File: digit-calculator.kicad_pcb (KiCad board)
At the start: 2 copper layers, 38.5 x 45 mm, 5 parts, among them J1 Trackball, J2 Battery, SW1 Switch, U1 XIAO-ESP32-C3-SMD

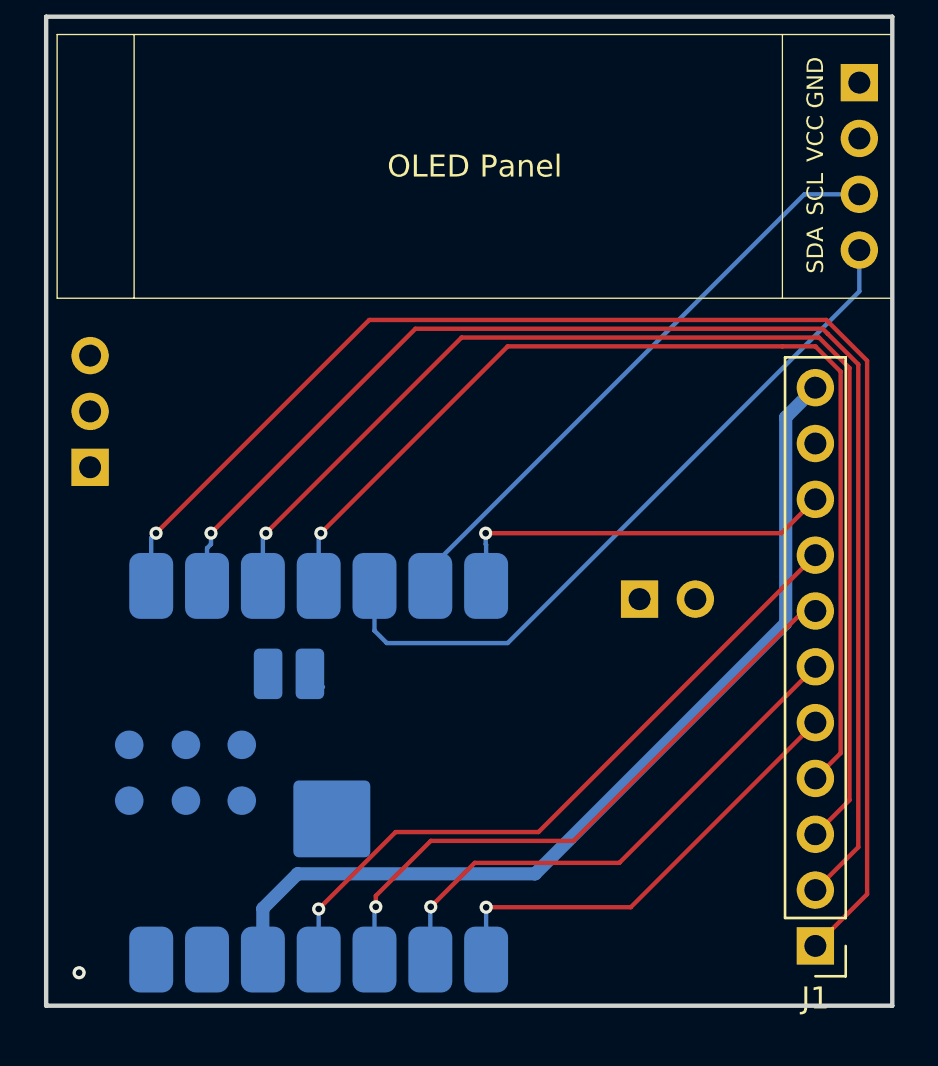
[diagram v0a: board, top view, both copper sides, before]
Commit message: Update wiring
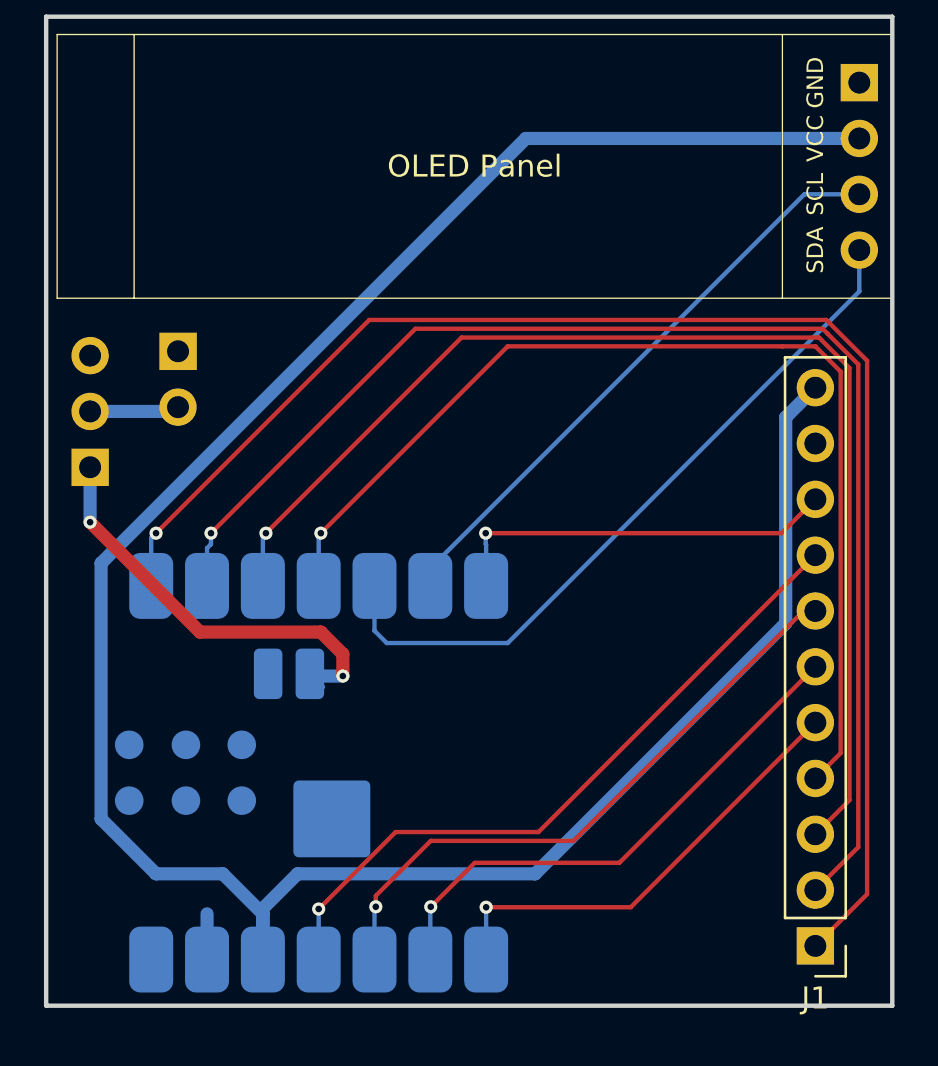
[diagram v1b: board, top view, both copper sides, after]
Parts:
- J2: value Battery -> - +
- moved J2 23.8 mm to (150.5, 64.7), turned to 180 degrees
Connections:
- SW1 pad 2: Net-(SW1-B) -> +BATT
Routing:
- net +3V3: track 42.8 -> 108.1 mm
- net +BATT: track 0.85 -> 24.0 mm, vias 0 -> 2
- net GND: track 0.00 -> 2.08 mm, vias 1 -> 0
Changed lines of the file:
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@@
 	(net 11 "/J_DOWN")
 	(net 12 "/J_RIGHT")
-	(net 13 "Net-(SW1-B)")
-	(net 14 "+BATT")
-	(net 15 "/SCL")
-	(net 16 "unconnected-(U1-VBUS-Pad14)")
+	(net 13 "+BATT")
+	(net 14 "/SCL")
+	(net 15 "unconnected-(U1-VBUS-Pad14)")
 	(footprint "Display:SSD1306-0.91-OLED-4pin-128x32"
 		(layer "F.Cu")
@@
 			(layers "*.Cu" "*.Mask")
 			(remove_unused_layers no)
-			(net 15 "/SCL")
+			(net 14 "/SCL")
 			(pinfunction "SCL")
 			(pintype "input")
@@
 	(footprint "Connector_PinHeader_2.54mm:PinHeader_1x02_P2.54mm_Vertical"
 		(layer "B.Cu")
-		(at 171.5 76 -90)
+		(at 150.5 64.725 180)
 		(descr "Through hole straight pin header, 1x02, 2.54mm pitch, single row")
 		(tags "Through hole pin header THT 1x02 2.54mm single row")
 		(property "Reference" "J2"
-			(at 0 2.38 90)
+			(at 0 2.38 0)
 			(layer "B.SilkS")
 			(effects
@@
 			)
 		)
-		(property "Value" "Battery"
-			(at 0 -4.92 90)
-			(layer "B.Fab")
-			(effects
-				(font
-					(size 1 1)
-					(thickness 0.15)
+		(property "Value" "- +"
+			(at -2.5 -1.275 90)
+			(layer "B.Fab")
+			(effects
+				(font
+					(size 1.4 1.4)
+					(thickness 0.175)
 				)
 				(justify mirror)
@@
 		)
 		(property "Datasheet" "~"
-			(at 0 0 90)
+			(at 0 0 0)
 			(layer "B.Fab")
 			(hide yes)
@@
 		)
 		(property "Description" "Generic connector, single row, 01x02, script generated (kicad-library-utils/schlib/autogen/connector/)"
-			(at 0 0 90)
+			(at 0 0 0)
 			(layer "B.Fab")
 			(hide yes)
@@
 		(attr through_hole)
 		(fp_line
+			(start 1.38 -1.27)
+			(end 1.38 -3.92)
+			(stroke
+				(width 0.12)
+				(type solid)
+			)
+			(layer "B.SilkS")
+		)
+		(fp_line
 			(start -1.38 1.38)
 			(end 0 1.38)
@@
 			(start -1.38 -1.27)
 			(end -1.38 -3.92)
-			(stroke
-				(width 0.12)
-				(type solid)
-			)
-			(layer "B.SilkS")
-		)
-		(fp_line
-			(start 1.38 -1.27)
-			(end 1.38 -3.92)
 			(stroke
 				(width 0.12)
@@
 		)
 		(fp_line
+			(start 1.27 1.27)
+			(end 1.27 -3.81)
+			(stroke
+				(width 0.1)
+				(type solid)
+			)
+			(layer "B.Fab")
+		)
+		(fp_line
+			(start 1.27 -3.81)
+			(end -1.27 -3.81)
+			(stroke
+				(width 0.1)
+				(type solid)
+			)
+			(layer "B.Fab")
+		)
+		(fp_line
 			(start -0.635 1.27)
 			(end 1.27 1.27)
@@
 		)
 		(fp_line
-			(start 1.27 1.27)
-			(end 1.27 -3.81)
-			(stroke
-				(width 0.1)
-				(type solid)
-			)
-			(layer "B.Fab")
-		)
-		(fp_line
 			(start -1.27 0.635)
 			(end -0.635 1.27)
@@
 			(layer "B.Fab")
 		)
-		(fp_line
-			(start 1.27 -3.81)
-			(end -1.27 -3.81)
-			(stroke
-				(width 0.1)
-				(type solid)
-			)
-			(layer "B.Fab")
-		)
 		(fp_text user "${REFERENCE}"
-			(at 0 -1.27 0)
+			(at 0 -1.27 90)
 			(layer "B.Fab")
 			(effects
@@
 		)
 		(pad "1" thru_hole rect
-			(at 0 0 270)
+			(at 0 0 180)
 			(size 1.7 1.7)
 			(drill 1)
@@
 		)
 		(pad "2" thru_hole circle
-			(at 0 -2.54 270)
+			(at 0 -2.54 180)
 			(size 1.7 1.7)
 			(drill 1)
 			(layers "*.Cu" "*.Mask")
 			(remove_unused_layers no)
-			(net 14 "+BATT")
+			(net 13 "+BATT")
 			(pinfunction "Pin_2")
 			(pintype "passive")
@@
 		)
 		(property "Value" "Switch"
-			(at 5 -5.5 0)
-			(layer "B.Fab")
+			(at -7 0.5 0)
+			(layer "B.Fab")
+			(hide yes)
 			(effects
 				(font
@@
 			(layers "*.Cu" "*.Mask")
 			(remove_unused_layers no)
-			(net 14 "+BATT")
+			(net 13 "+BATT")
 			(pinfunction "A")
 			(pintype "passive")
@@
 			(layers "*.Cu" "*.Mask")
 			(remove_unused_layers no)
-			(net 13 "Net-(SW1-B)")
+			(net 13 "+BATT")
 			(pinfunction "B")
 			(pintype "passive")
@@
 			(layers "B.Cu" "B.Mask" "B.Paste")
 			(roundrect_rratio 0.25)
-			(net 15 "/SCL")
+			(net 14 "/SCL")
 			(pinfunction "GPIO7_D5_SCL")
 			(pintype "passive")
@@
 			(layers "B.Cu" "B.Mask" "B.Paste")
 			(roundrect_rratio 0.25)
-			(net 16 "unconnected-(U1-VBUS-Pad14)")
+			(net 15 "unconnected-(U1-VBUS-Pad14)")
 			(pinfunction "VBUS")
 			(pintype "passive")
@@
 			(layers "B.Cu" "B.Mask" "B.Paste")
 			(roundrect_rratio 0.1923076923)
-			(net 14 "+BATT")
+			(net 13 "+BATT")
 		)
 		(pad "17" smd roundrect
@@
 		(layer "Edge.Cuts")
 	)
-	(via
-		(at 146 93)
-		(size 0.6)
-		(drill 0.3)
-		(layers "F.Cu" "B.Cu")
-		(free yes)
+	(segment
+		(start 151.82 92.4)
+		(end 151.82 90.32)
+		(width 0.6)
+		(layer "B.Cu")
 		(net 1)
+	)
+	(segment
+		(start 166.327214 55.04)
+		(end 147 74.367214)
+		(width 0.6)
+		(layer "B.Cu")
+		(net 2)
 	)
 	(segment
@@
 	)
 	(segment
+		(start 152.538 88.5)
+		(end 149.5 88.5)
+		(width 0.6)
+		(layer "B.Cu")
+		(net 2)
+	)
+	(segment
 		(start 178.149 67.731)
 		(end 179.5 66.38)
@@
 	)
 	(segment
-		(start 154.36 90.07855)
-		(end 155.93855 88.5)
+		(start 155.93855 88.5)
+		(end 154.36 90.07855)
 		(width 0.6)
 		(layer "B.Cu")
@@
 	)
 	(segment
+		(start 154.36 90.07855)
+		(end 154.36 92.4)
+		(width 0.6)
+		(layer "B.Cu")
+		(net 2)
+	)
+	(segment
 		(start 178.149 77.099603)
 		(end 178.149 67.731)
@@
 	)
 	(segment
-		(start 154.36 92.4)
-		(end 154.36 90.07855)
+		(start 147 74.367214)
+		(end 147 86)
+		(width 0.6)
+		(layer "B.Cu")
+		(net 2)
+	)
+	(segment
+		(start 181.5 55.04)
+		(end 166.327214 55.04)
+		(width 0.6)
+		(layer "B.Cu")
+		(net 2)
+	)
+	(segment
+		(start 154.36 90.322)
+		(end 154.36 92.4)
+		(width 0.6)
+		(layer "B.Cu")
+		(net 2)
+	)
+	(segment
+		(start 149.5 88.5)
+		(end 147 86)
+		(width 0.6)
+		(layer "B.Cu")
+		(net 2)
+	)
+	(segment
+		(start 152.538 88.5)
+		(end 154.36 90.322)
 		(width 0.6)
 		(layer "B.Cu")
@@
 	)
 	(segment
+		(start 151.5 77.5)
+		(end 157 77.5)
+		(width 0.6)
+		(layer "F.Cu")
+		(net 13)
+	)
+	(segment
+		(start 158 78.5)
+		(end 158 79.5)
+		(width 0.6)
+		(layer "F.Cu")
+		(net 13)
+	)
+	(segment
+		(start 146.5 72.5)
+		(end 151.5 77.5)
+		(width 0.6)
+		(layer "F.Cu")
+		(net 13)
+	)
+	(segment
+		(start 157 77.5)
+		(end 158 78.5)
+		(width 0.6)
+		(layer "F.Cu")
+		(net 13)
+	)
+	(via
+		(at 146.5 72.5)
+		(size 0.6)
+		(drill 0.3)
+		(layers "F.Cu" "B.Cu")
+		(net 13)
+	)
+	(via
+		(at 158 79.5)
+		(size 0.6)
+		(drill 0.3)
+		(layers "F.Cu" "B.Cu")
+		(free yes)
+		(net 13)
+	)
+	(segment
+		(start 150.305 67.46)
+		(end 150.5 67.265)
+		(width 0.6)
+		(layer "B.Cu")
+		(net 13)
+	)
+	(segment
+		(start 156.6 79.5)
+		(end 156.5 79.4)
+		(width 0.6)
+		(layer "B.Cu")
+		(net 13)
+	)
+	(segment
+		(start 158 79.5)
+		(end 156.6 79.5)
+		(width 0.6)
+		(layer "B.Cu")
+		(net 13)
+	)
+	(segment
 		(start 156.5 79.4)
 		(end 157.1 80)
 		(width 0.2)
 		(layer "B.Cu")
-		(net 14)
+		(net 13)
+	)
+	(segment
+		(start 146.5 67.46)
+		(end 150.305 67.46)
+		(width 0.6)
+		(layer "B.Cu")
+		(net 13)
+	)
+	(segment
+		(start 146.5 70)
+		(end 146.5 72.5)
+		(width 0.6)
+		(layer "B.Cu")
+		(net 13)
 	)
 	(segment
@@
 		(width 0.2)
 		(layer "B.Cu")
-		(net 15)
+		(net 14)
 	)
 	(segment
@@
 		(width 0.2)
 		(layer "B.Cu")
-		(net 15)
+		(net 14)
 	)
 	(segment
@@
 		(width 0.2)
 		(layer "B.Cu")
-		(net 15)
+		(net 14)
 	)
 	(zone

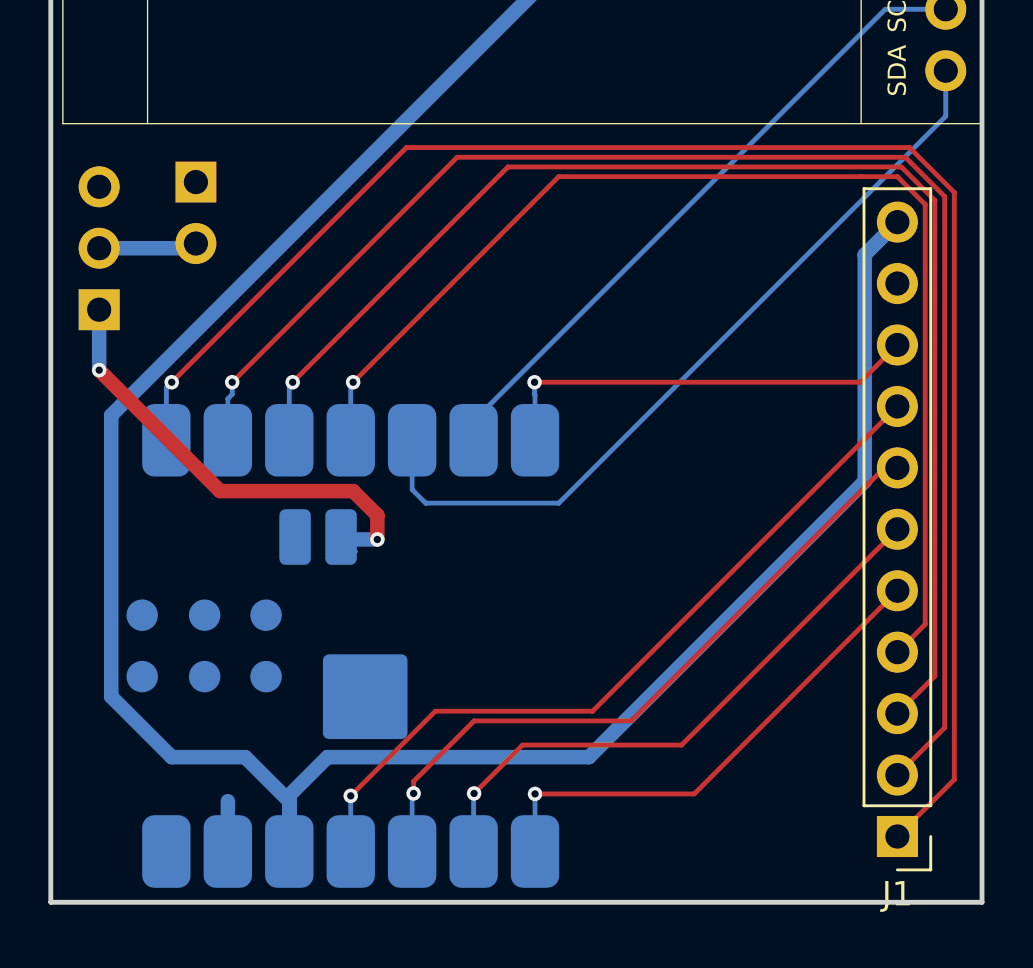
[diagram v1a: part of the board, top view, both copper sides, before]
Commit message: fix ground plane DRC
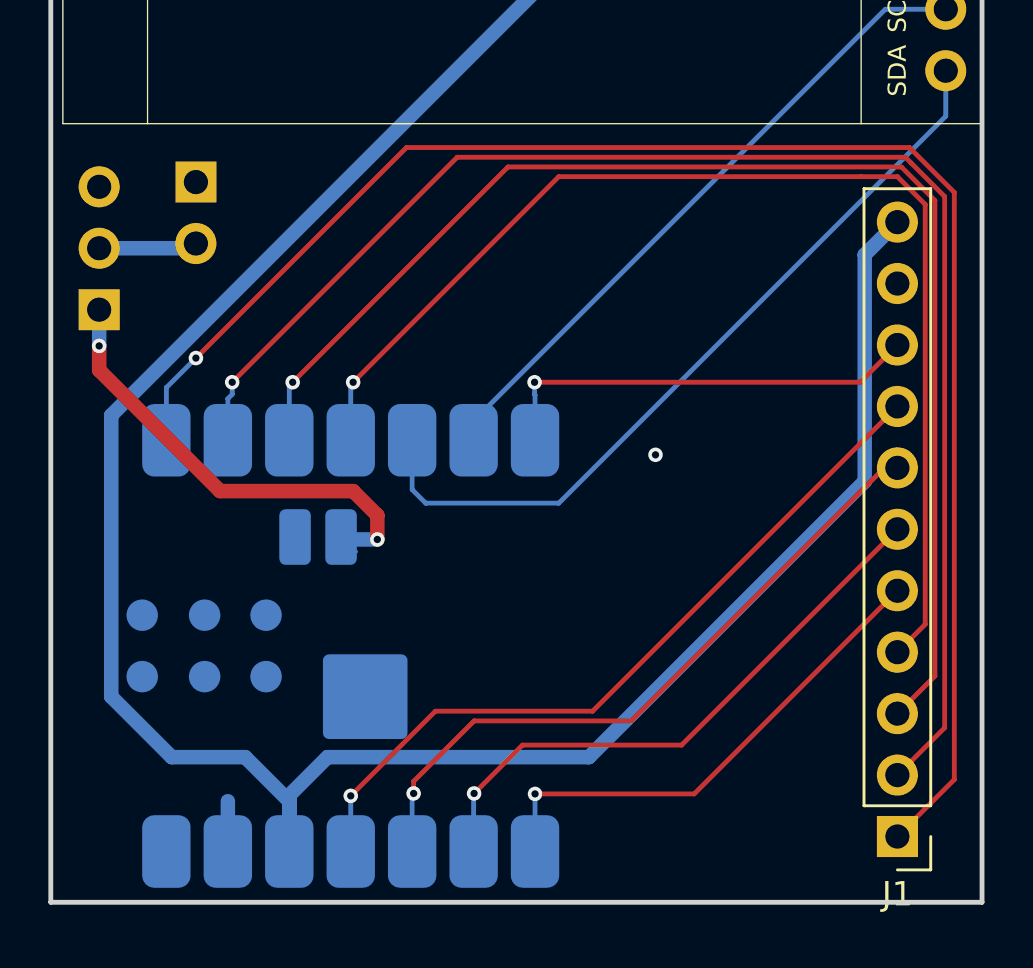
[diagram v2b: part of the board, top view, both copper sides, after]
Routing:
- net GND: vias 0 -> 1
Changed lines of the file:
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@@
 		(layer "Edge.Cuts")
+	)
+	(via
+		(at 169.5 76)
+		(size 0.6)
+		(drill 0.3)
+		(layers "F.Cu" "B.Cu")
+		(free yes)
+		(net 1)
 	)
 	(segment
@@
 	)
 	(segment
+		(start 179.9983 63.297)
+		(end 181.854 65.1527)
+		(width 0.2)
+		(layer "F.Cu")
+		(net 4)
+	)
+	(segment
 		(start 181.854 65.1527)
+		(end 181.854 89.426)
+		(width 0.2)
+		(layer "F.Cu")
+		(net 4)
+	)
+	(segment
+		(start 150.5 72)
+		(end 159.203 63.297)
+		(width 0.2)
+		(layer "F.Cu")
+		(net 4)
+	)
+	(segment
+		(start 159.203 63.297)
 		(end 179.9983 63.297)
 		(width 0.2)
@@
 	)
 	(segment
-		(start 159.203 63.297)
-		(end 149.5 73)
+		(start 181.854 89.426)
+		(end 179.5 91.78)
 		(width 0.2)
 		(layer "F.Cu")
 		(net 4)
 	)
-	(segment
-		(start 179.9983 63.297)
-		(end 159.203 63.297)
-		(width 0.2)
-		(layer "F.Cu")
-		(net 4)
-	)
-	(segment
-		(start 181.854 89.426)
-		(end 181.854 65.1527)
-		(width 0.2)
-		(layer "F.Cu")
-		(net 4)
-	)
-	(segment
-		(start 179.5 91.78)
-		(end 181.854 89.426)
-		(width 0.2)
-		(layer "F.Cu")
-		(net 4)
-	)
-	(via
-		(at 149.5 73)
-		(size 0.6)
-		(drill 0.3)
-		(layers "F.Cu" "B.Cu")
-		(net 4)
-	)
-	(segment
-		(start 149.5 73)
-		(end 149.28 73.22)
-		(width 0.2)
-		(layer "B.Cu")
+	(via
+		(at 150.5 72)
+		(size 0.6)
+		(drill 0.3)
+		(layers "F.Cu" "B.Cu")
 		(net 4)
 	)
@@
 	)
 	(segment
+		(start 150.5 72)
+		(end 149.28 73.22)
+		(width 0.2)
+		(layer "B.Cu")
+		(net 4)
+	)
+	(segment
 		(start 180.651 83.009)
 		(end 180.651 65.651)
@@
 	)
 	(segment
+		(start 146.5 72.5)
+		(end 151.5 77.5)
+		(width 0.6)
+		(layer "F.Cu")
+		(net 13)
+	)
+	(segment
 		(start 151.5 77.5)
 		(end 157 77.5)
@@
 	)
 	(segment
-		(start 146.5 72.5)
-		(end 151.5 77.5)
+		(start 146.5 71.5)
+		(end 146.5 72.5)
 		(width 0.6)
 		(layer "F.Cu")
@@
 	)
 	(via
-		(at 146.5 72.5)
+		(at 146.5 71.5)
 		(size 0.6)
 		(drill 0.3)
@@
 	(segment
 		(start 146.5 70)
-		(end 146.5 72.5)
-		(width 0.6)
-		(layer "B.Cu")
+		(end 146.5 71.5)
+		(width 0.6)
+		(layer "B.Cu")

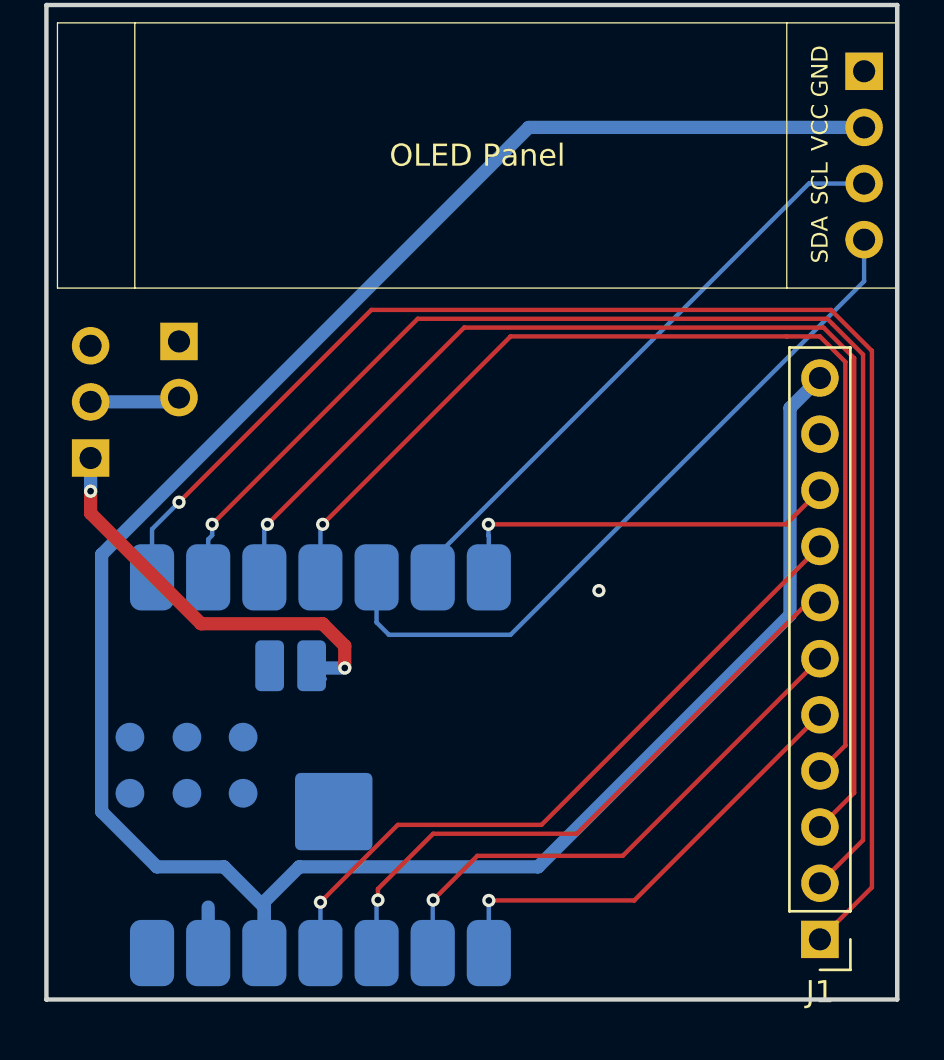
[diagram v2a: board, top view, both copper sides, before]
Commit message: add silkscreen
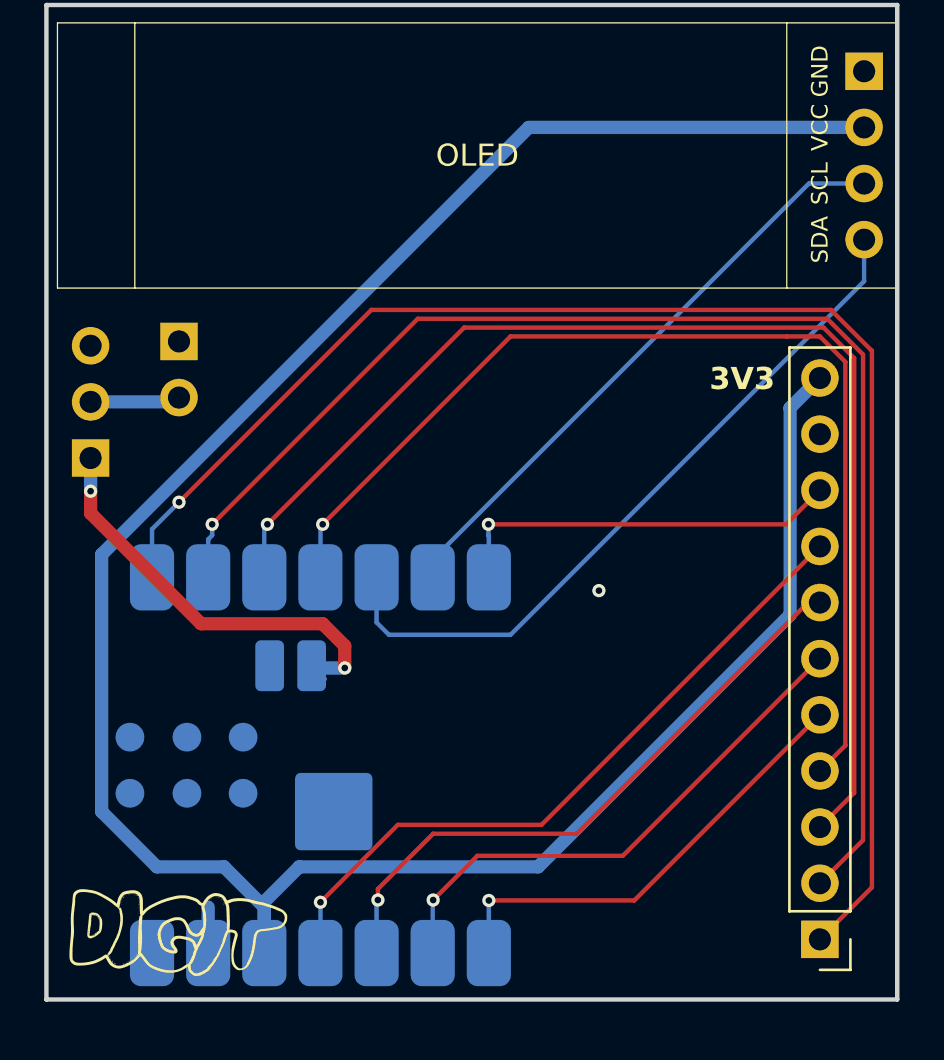
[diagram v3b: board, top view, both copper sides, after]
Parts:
- added G***: LOGO, LOGO, F.Cu at (150.5, 91.5)
- added G***: LOGO, LOGO, B.Cu at (173.0, 55.0)
- J1: value Trackball -> 3V3
- U1: value XIAO-ESP32-C3-SMD -> XIAO this side
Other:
- board text added: "3V3"
- board text added: "switch →"
